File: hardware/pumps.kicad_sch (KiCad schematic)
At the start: 8 parts, among them Q5 PMV450ENEA

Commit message: Add the Cube project
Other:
- note removed: "TODO: Add a mosfet driver"
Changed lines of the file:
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@@
   (title_block
     (title "Pumps")
-    (date "2023-06-06")
+    (date "2023-07-01")
     (rev "${REVISION}")
     (company "Author: I. Kajdan")
@@
     (effects (font (size 1.27 1.27)) (justify left bottom))
   )
-  (text "TODO: Add a mosfet driver" (at 139.7 128.27 0)
-    (effects (font (size 1.27 1.27)) (justify left bottom))
-  )
   (hierarchical_label "IN_L" (shape input) (at 106.68 106.68 180) (fields_autoplaced)
     (effects (font (size 1.27 1.27)) (justify right))
@@
         )
         (path "/b652b05a-4e3d-4ad1-b032-18886abe7d45/2f82735d-d185-44cc-bb86-fc399780134d"
+          (reference "R33") (unit 1)
+        )
+      )
+    )
+  )
+  (symbol (lib_id "Device:R_Small") (at 180.34 96.52 0) (unit 1)
+    (in_bom yes) (on_board yes) (dnp no)
+    (property "Reference" "R?" (at 181.8386 94.0816 0)
+      (effects (font (size 1.27 1.27)) (justify left))
+    )
+    (property "Value" "0R" (at 181.8386 96.393 0)
+      (effects (font (size 1.27 1.27)) (justify left))
+    )
+    (property "Footprint" "Resistor_SMD:R_0603_1608Metric" (at 180.34 96.52 0)
+      (effects (font (size 1.27 1.27)) hide)
+    )
+    (property "Datasheet" "~" (at 180.34 96.52 0)
+      (effects (font (size 1.27 1.27)) hide)
+    )
+    (property "Case" "0603" (at 181.61 99.06 0)
+      (effects (font (size 1.27 1.27)) (justify left))
+    )
+    (pin "1")
+    (pin "2")
+    (instances
+      (project "DV_ASSI"
+        (path "/9ea404c5-06ed-4d33-a203-54354d60e659/00000000-0000-0000-0000-00005fb03161"
+          (reference "R?") (unit 1)
+        )
+      )
+      (project "rearbox"
+        (path "/b652b05a-4e3d-4ad1-b032-18886abe7d45/23ffbfb4-d932-48bb-a16b-e7ed705895f1"
+          (reference "R?") (unit 1)
+        )
+        (path "/b652b05a-4e3d-4ad1-b032-18886abe7d45/91248db3-ac16-4fb7-9cfe-25145bb94249"
+          (reference "R?") (unit 1)
+        )
+        (path "/b652b05a-4e3d-4ad1-b032-18886abe7d45/2f82735d-d185-44cc-bb86-fc399780134d"
+          (reference "R37") (unit 1)
+        )
+      )
+    )
+  )
+  (symbol (lib_id "Device:R_Small") (at 175.26 114.3 270) (unit 1)
+    (in_bom yes) (on_board yes) (dnp no)
+    (property "Reference" "R?" (at 175.26 111.76 90)
+      (effects (font (size 1.27 1.27)))
+    )
+    (property "Value" "R_Small" (at 175.26 116.84 90)
+      (effects (font (size 1.27 1.27)))
+    )
+    (property "Footprint" "Resistor_SMD:R_0402_1005Metric" (at 175.26 114.3 0)
+      (effects (font (size 1.27 1.27)) hide)
+    )
+    (property "Datasheet" "~" (at 175.26 114.3 0)
+      (effects (font (size 1.27 1.27)) hide)
+    )
+    (pin "1")
+    (pin "2")
+    (instances
+      (project "DV_ASSI"
+        (path "/9ea404c5-06ed-4d33-a203-54354d60e659/00000000-0000-0000-0000-00005fb03161"
+          (reference "R?") (unit 1)
+        )
+      )
+      (project "rearbox"
+        (path "/b652b05a-4e3d-4ad1-b032-18886abe7d45/23ffbfb4-d932-48bb-a16b-e7ed705895f1"
+          (reference "R?") (unit 1)
+        )
+        (path "/b652b05a-4e3d-4ad1-b032-18886abe7d45/91248db3-ac16-4fb7-9cfe-25145bb94249"
+          (reference "R?") (unit 1)
+        )
+        (path "/b652b05a-4e3d-4ad1-b032-18886abe7d45/2f82735d-d185-44cc-bb86-fc399780134d"
+          (reference "R36") (unit 1)
+        )
+      )
+    )
+  )
+  (symbol (lib_id "Device:R_Small") (at 127 96.52 0) (unit 1)
+    (in_bom yes) (on_board yes) (dnp no)
+    (property "Reference" "R?" (at 128.4986 94.0816 0)
+      (effects (font (size 1.27 1.27)) (justify left))
+    )
+    (property "Value" "0R" (at 128.4986 96.393 0)
+      (effects (font (size 1.27 1.27)) (justify left))
+    )
+    (property "Footprint" "Resistor_SMD:R_0603_1608Metric" (at 127 96.52 0)
+      (effects (font (size 1.27 1.27)) hide)
+    )
+    (property "Datasheet" "~" (at 127 96.52 0)
+      (effects (font (size 1.27 1.27)) hide)
+    )
+    (property "Case" "0603" (at 128.27 99.06 0)
+      (effects (font (size 1.27 1.27)) (justify left))
+    )
+    (pin "1")
+    (pin "2")
+    (instances
+      (project "DV_ASSI"
+        (path "/9ea404c5-06ed-4d33-a203-54354d60e659/00000000-0000-0000-0000-00005fb03161"
+          (reference "R?") (unit 1)
+        )
+      )
+      (project "rearbox"
+        (path "/b652b05a-4e3d-4ad1-b032-18886abe7d45/23ffbfb4-d932-48bb-a16b-e7ed705895f1"
+          (reference "R?") (unit 1)
+        )
+        (path "/b652b05a-4e3d-4ad1-b032-18886abe7d45/91248db3-ac16-4fb7-9cfe-25145bb94249"
+          (reference "R?") (unit 1)
+        )
+        (path "/b652b05a-4e3d-4ad1-b032-18886abe7d45/2f82735d-d185-44cc-bb86-fc399780134d"
           (reference "R34") (unit 1)
-        )
-      )
-    )
-  )
-  (symbol (lib_id "Device:R_Small") (at 180.34 96.52 0) (unit 1)
-    (in_bom yes) (on_board yes) (dnp no)
-    (property "Reference" "R?" (at 181.8386 94.0816 0)
-      (effects (font (size 1.27 1.27)) (justify left))
-    )
-    (property "Value" "0R" (at 181.8386 96.393 0)
-      (effects (font (size 1.27 1.27)) (justify left))
-    )
-    (property "Footprint" "Resistor_SMD:R_0603_1608Metric" (at 180.34 96.52 0)
-      (effects (font (size 1.27 1.27)) hide)
-    )
-    (property "Datasheet" "~" (at 180.34 96.52 0)
-      (effects (font (size 1.27 1.27)) hide)
-    )
-    (property "Case" "0603" (at 181.61 99.06 0)
-      (effects (font (size 1.27 1.27)) (justify left))
-    )
-    (pin "1")
-    (pin "2")
-    (instances
-      (project "DV_ASSI"
-        (path "/9ea404c5-06ed-4d33-a203-54354d60e659/00000000-0000-0000-0000-00005fb03161"
-          (reference "R?") (unit 1)
-        )
-      )
-      (project "rearbox"
-        (path "/b652b05a-4e3d-4ad1-b032-18886abe7d45/23ffbfb4-d932-48bb-a16b-e7ed705895f1"
-          (reference "R?") (unit 1)
-        )
-        (path "/b652b05a-4e3d-4ad1-b032-18886abe7d45/91248db3-ac16-4fb7-9cfe-25145bb94249"
-          (reference "R?") (unit 1)
-        )
-        (path "/b652b05a-4e3d-4ad1-b032-18886abe7d45/2f82735d-d185-44cc-bb86-fc399780134d"
-          (reference "R38") (unit 1)
-        )
-      )
-    )
-  )
-  (symbol (lib_id "Device:R_Small") (at 175.26 114.3 270) (unit 1)
-    (in_bom yes) (on_board yes) (dnp no)
-    (property "Reference" "R?" (at 175.26 111.76 90)
-      (effects (font (size 1.27 1.27)))
-    )
-    (property "Value" "R_Small" (at 175.26 116.84 90)
-      (effects (font (size 1.27 1.27)))
-    )
-    (property "Footprint" "Resistor_SMD:R_0402_1005Metric" (at 175.26 114.3 0)
-      (effects (font (size 1.27 1.27)) hide)
-    )
-    (property "Datasheet" "~" (at 175.26 114.3 0)
-      (effects (font (size 1.27 1.27)) hide)
-    )
-    (pin "1")
-    (pin "2")
-    (instances
-      (project "DV_ASSI"
-        (path "/9ea404c5-06ed-4d33-a203-54354d60e659/00000000-0000-0000-0000-00005fb03161"
-          (reference "R?") (unit 1)
-        )
-      )
-      (project "rearbox"
-        (path "/b652b05a-4e3d-4ad1-b032-18886abe7d45/23ffbfb4-d932-48bb-a16b-e7ed705895f1"
-          (reference "R?") (unit 1)
-        )
-        (path "/b652b05a-4e3d-4ad1-b032-18886abe7d45/91248db3-ac16-4fb7-9cfe-25145bb94249"
-          (reference "R?") (unit 1)
-        )
-        (path "/b652b05a-4e3d-4ad1-b032-18886abe7d45/2f82735d-d185-44cc-bb86-fc399780134d"
-          (reference "R37") (unit 1)
-        )
-      )
-    )
-  )
-  (symbol (lib_id "Device:R_Small") (at 127 96.52 0) (unit 1)
-    (in_bom yes) (on_board yes) (dnp no)
-    (property "Reference" "R?" (at 128.4986 94.0816 0)
-      (effects (font (size 1.27 1.27)) (justify left))
-    )
-    (property "Value" "0R" (at 128.4986 96.393 0)
-      (effects (font (size 1.27 1.27)) (justify left))
-    )
-    (property "Footprint" "Resistor_SMD:R_0603_1608Metric" (at 127 96.52 0)
-      (effects (font (size 1.27 1.27)) hide)
-    )
-    (property "Datasheet" "~" (at 127 96.52 0)
-      (effects (font (size 1.27 1.27)) hide)
-    )
-    (property "Case" "0603" (at 128.27 99.06 0)
-      (effects (font (size 1.27 1.27)) (justify left))
-    )
-    (pin "1")
-    (pin "2")
-    (instances
-      (project "DV_ASSI"
-        (path "/9ea404c5-06ed-4d33-a203-54354d60e659/00000000-0000-0000-0000-00005fb03161"
-          (reference "R?") (unit 1)
-        )
-      )
-      (project "rearbox"
-        (path "/b652b05a-4e3d-4ad1-b032-18886abe7d45/23ffbfb4-d932-48bb-a16b-e7ed705895f1"
-          (reference "R?") (unit 1)
-        )
-        (path "/b652b05a-4e3d-4ad1-b032-18886abe7d45/91248db3-ac16-4fb7-9cfe-25145bb94249"
-          (reference "R?") (unit 1)
-        )
-        (path "/b652b05a-4e3d-4ad1-b032-18886abe7d45/2f82735d-d185-44cc-bb86-fc399780134d"
-          (reference "R35") (unit 1)
         )
       )
@@
         )
         (path "/b652b05a-4e3d-4ad1-b032-18886abe7d45/2f82735d-d185-44cc-bb86-fc399780134d"
-          (reference "R33") (unit 1)
+          (reference "R32") (unit 1)
         )
       )
@@
         )
         (path "/b652b05a-4e3d-4ad1-b032-18886abe7d45/2f82735d-d185-44cc-bb86-fc399780134d"
-          (reference "R36") (unit 1)
-        )
-      )
+          (reference "R35") (unit 1)
+        )
+      )

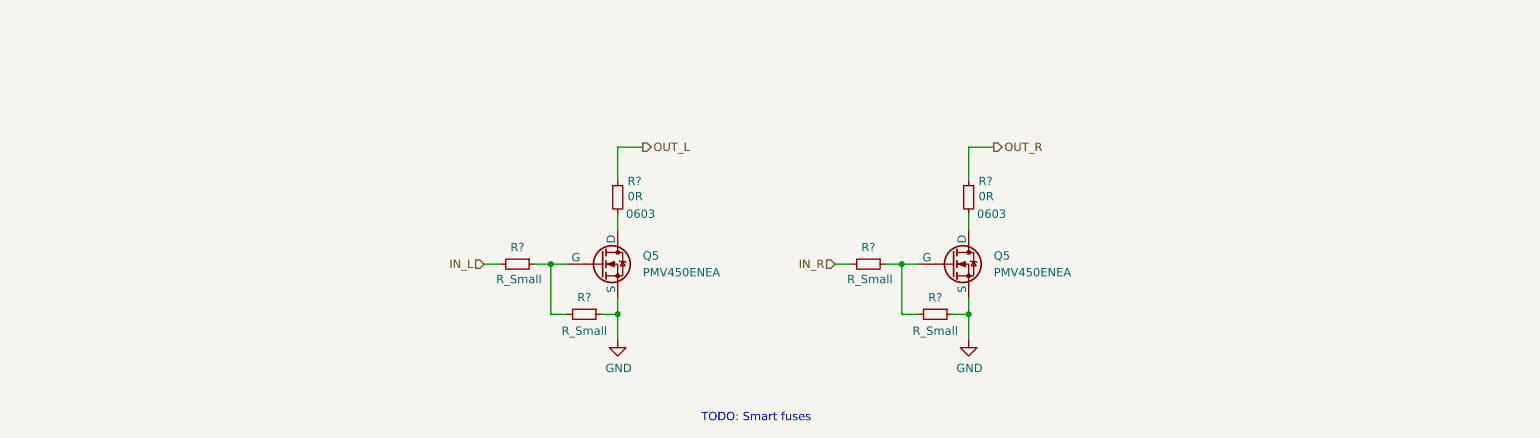
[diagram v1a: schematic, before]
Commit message: Improve the schematic
- add anti-aliasing filters
- rearrange the main connector signals
- improve the power filtering
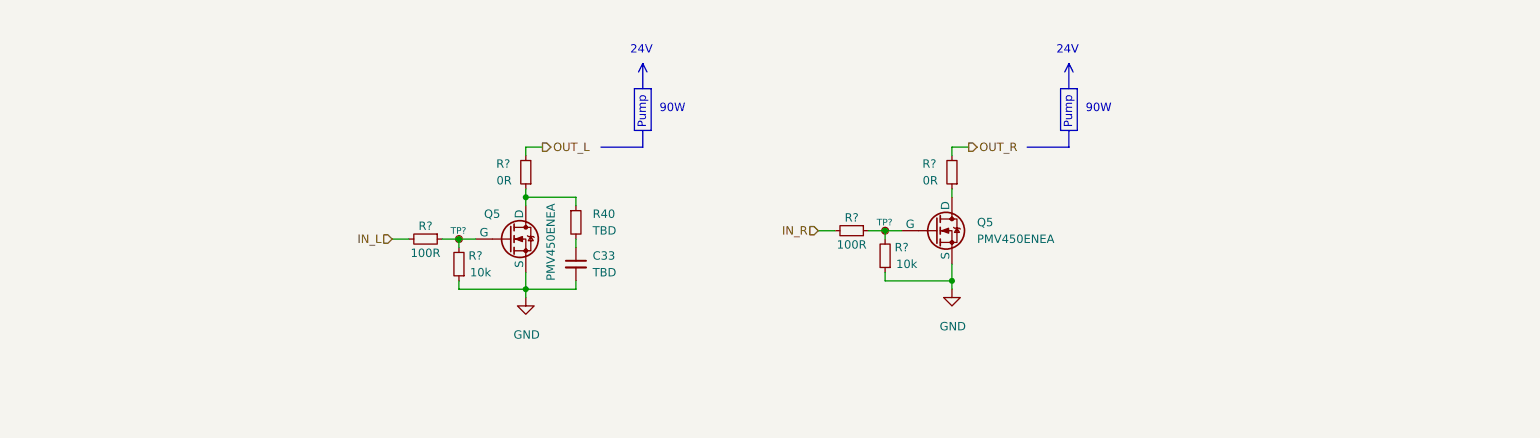
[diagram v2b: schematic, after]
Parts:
- removed Q5 (x2): PMV450ENEA, symbol Simulation_SPICE:NMOS
- removed R? (x4): R_Small, Resistor_SMD:R_0402_1005Metric, symbol Device:R_Small
- removed R? (x2): 0R, Resistor_SMD:R_0603_1608Metric, symbol Device:R_Small
- added C33: TBD, Capacitor_SMD:C_0603_1608Metric, symbol Device:C_Small
- added Q5 (x2): PMV450ENEA, symbol Simulation_SPICE:NMOS
- added R40: TBD, Resistor_SMD:R_0603_1608Metric, symbol Device:R_Small
- added R? (x2): 0R, Resistor_SMD:R_0603_1608Metric, symbol Device:R_Small
- added R? (x2): 100R, Resistor_SMD:R_0603_1608Metric, symbol Device:R_Small
- added R? (x2): 10k, Resistor_SMD:R_0603_1608Metric, symbol Device:R_Small
- added TP? (x2): TestPoint_Small, TestPoint:TestPoint_Pad_D1.0mm, symbol Connector:TestPoint_Small
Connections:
- net GND: now also C33.2, Q5.3 (S), Q5.3 (S), R?.1, R?.1
- net IN_L: now also R?.2
- net IN_R: now also R?.2
- net OUT_L: now also R?.2
- net OUT_R: now also R?.2
- new net: Q5.2 (G), R?.1, R?.2, TP?.1 (x2)
- new net: Q5.1 (D), R40.1, R?.1
- new net: Q5.1 (D), R?.1
- new net: C33.1, R40.2
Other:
- note added: "24V"
- note added: "90W"
- note added: "Pump"
- note removed: "TODO: Smart fuses"

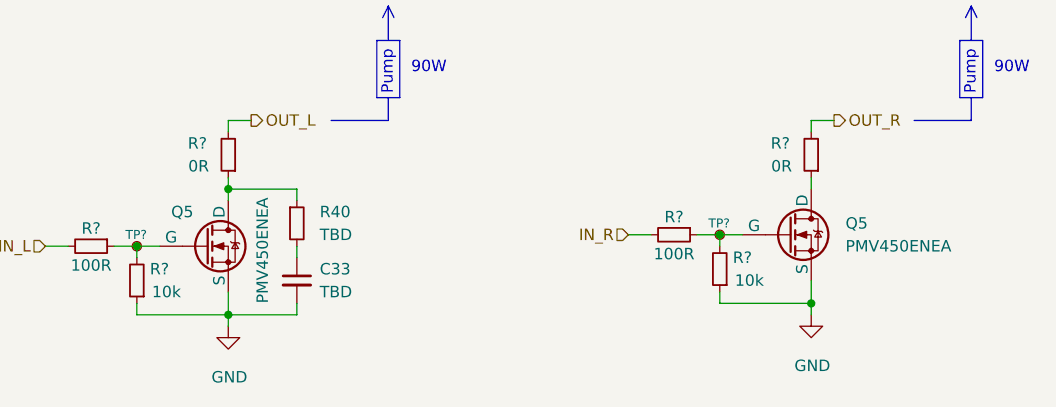
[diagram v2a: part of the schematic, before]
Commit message: Set component values
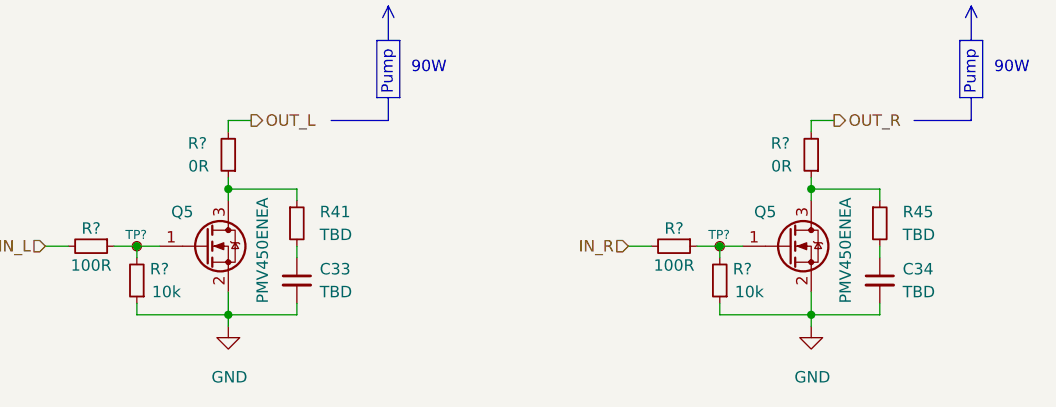
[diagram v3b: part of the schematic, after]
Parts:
- removed Q5: PMV450ENEA, symbol Simulation_SPICE:NMOS
- added C34: TBD, Capacitor_SMD:C_0603_1608Metric, symbol Device:C_Small
- added Q5: PMV450ENEA, symbol Device:Q_NMOS_GSD
- added R45: TBD, Resistor_SMD:R_0603_1608Metric, symbol Device:R_Small
- Q5: symbol Simulation_SPICE:NMOS -> Device:Q_NMOS_GSD
- renumbered R40 to R41
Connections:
- net GND: now also Q5.2 (S), C34.2, Q5.2 (S); no longer Q5.3 (S)
- net at R?.1, R?.2, TP?.1: now also Q5.1 (G); no longer Q5.2 (G)
- net at R41.1, R?.1: now also Q5.3 (D); no longer Q5.1 (D)
- net at R?.1: now also Q5.3 (D), R45.1
- net at R?.1, R?.2, TP?.1: now also Q5.1 (G)
- new net: C34.1, R45.2
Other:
- moved on the sheet: R?, TP?

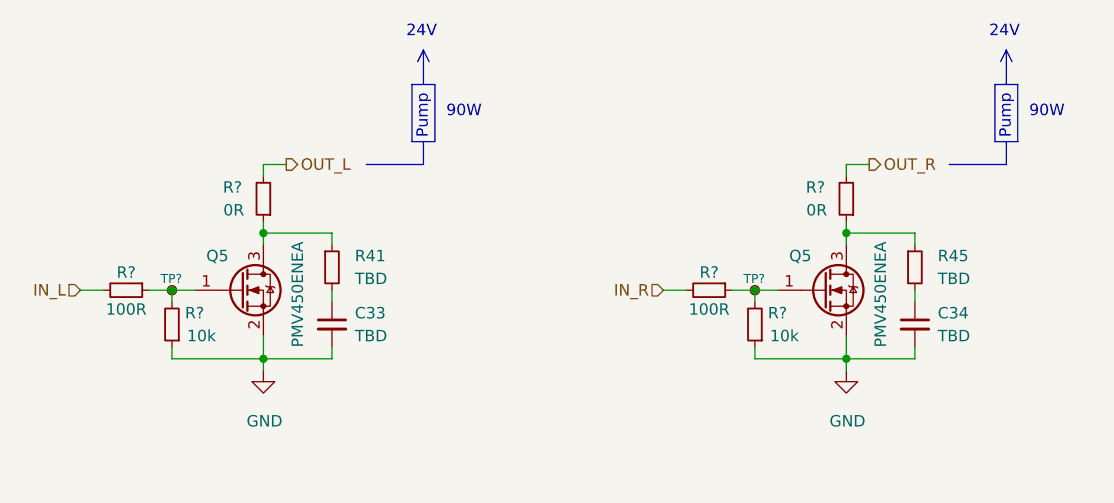
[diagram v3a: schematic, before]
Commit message: Improve the schematic according to the feedback
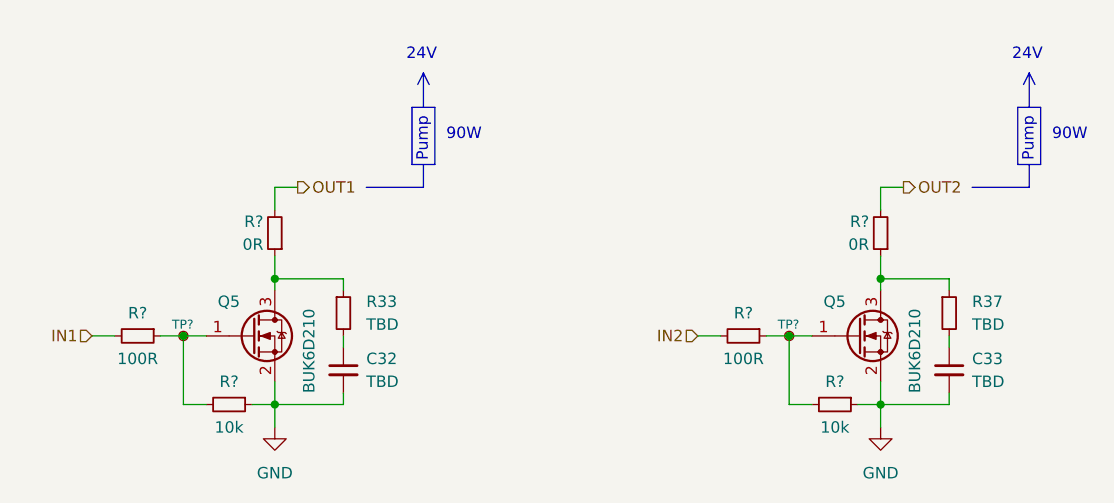
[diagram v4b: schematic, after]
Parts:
- removed R? (x2): 10k, Resistor_SMD:R_0603_1608Metric, symbol Device:R_Small
- added R? (x2): 10k, Resistor_SMD:R_0603_1608Metric, symbol Device:R_Small
- Q5: value PMV450ENEA -> BUK6D210; footprint (none) -> Package_DFN_QFN:Diodes_UDFN2020-6_Type-F
- renumbered C33 to C32, C34 to C33, R41 to R33, R45 to R37
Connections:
- net GND: now also R?.1, R?.1
- net at Q5.1 (G), R?.1, TP?.1: now also R?.2 (x2)
- net IN_L renamed IN1
- net IN_R renamed IN2
- net OUT_L renamed OUT1
- net OUT_R renamed OUT2
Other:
- moved on the sheet: C32, C33, Q5, R33, R37, R?, TP?
